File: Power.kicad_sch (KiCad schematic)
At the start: 18 parts, among them J4 Conn_01x02, SW2 SW_Push, U6 NPM1300-QEAA-R7

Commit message: Switch inductors
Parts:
- removed L1, L2: LQM2HPN2R2MG0L, LQM:IND_LQM2HPN2R2MG0L_MUR, symbol 2026-04-16_01-05-19:LQM2HPN2R2MG0L
- added L3, L4: 2.2uH, Inductor_SMD:L_0805_2012Metric, symbol Device:L_Small
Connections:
- net +1V8: now also L3.1
- net +3V0: now also L4.1
- net SW1: now also L3.2
- net SW2: now also L4.2

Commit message: WIP changes
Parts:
- SW2: footprint SKRPACE:SW_SKRPACE010_AAL -> Resistor_SMD:R_0805_2012Metric
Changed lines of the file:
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@@
 			)
 		)
-		(property "Footprint" "SKRPACE:SW_SKRPACE010_AAL"
+		(property "Footprint" "Resistor_SMD:R_0805_2012Metric"
 			(at 77.47 119.38 0)
 			(hide yes)

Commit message: Added Backpack Integration + Layout V1
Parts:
- SW2: now left out of the parts list

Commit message: Began Backpack Removal to Lower Profile
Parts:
- C10, C22: Price 0.008USD -> (none)
- C11, C16, C17, C18, C19, C20: Price 0.009USD -> (none)
- C15: Price 0.006USD -> (none)
- R12, R13: Price 0.004USD -> (none)

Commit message: Flipped switches + Heart Rate, Moving Battery
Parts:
- J4: footprint Connector_JST:JST_PH_S2B-PH-K_1x02_P2.00mm_Horizontal -> Smart_Watch:MOLEX_0781710002
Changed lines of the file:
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@@
 			)
 		)
-		(property "Footprint" "Connector_JST:JST_PH_S2B-PH-K_1x02_P2.00mm_Horizontal"
+		(property "Footprint" "Smart_Watch:MOLEX_0781710002"
 			(at 49.53 76.2 0)
 			(hide yes)

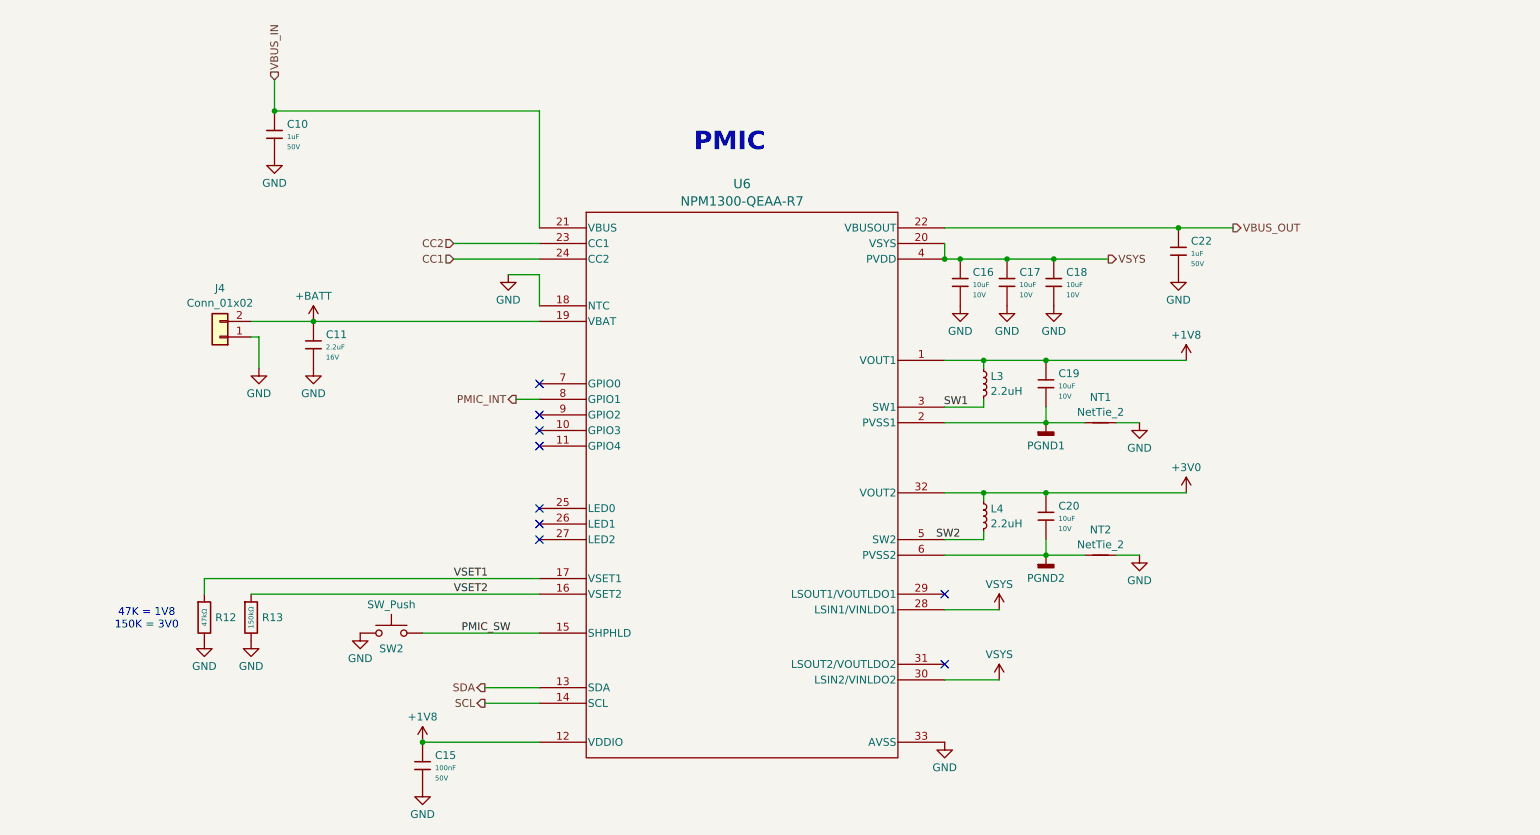
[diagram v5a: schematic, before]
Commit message: Added Test Points and Changed to Top Mounted USBC
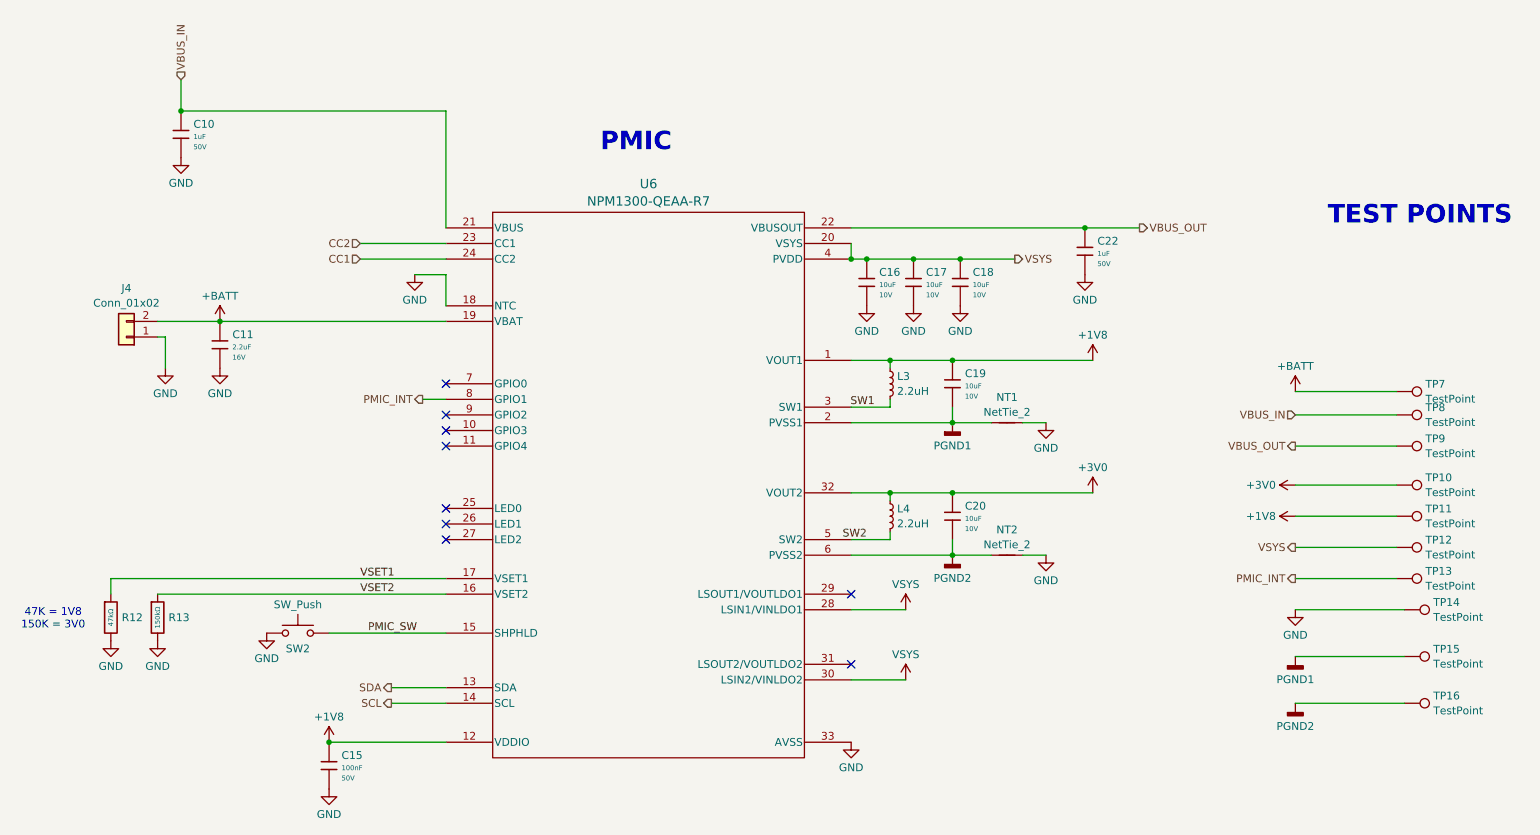
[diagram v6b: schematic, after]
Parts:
- added TP10, TP11, TP12, TP13, TP14, TP15, TP16, TP7, TP8, TP9: TestPoint, TestPoint:TestPoint_Pad_1.0x1.0mm, symbol Connector:TestPoint
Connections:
- net +1V8: now also TP11.1
- net +3V0: now also TP10.1
- net +BATT: now also TP7.1
- net GND: now also TP14.1
- net PGND1: now also TP15.1
- net PGND2: now also TP16.1
- net PMIC_INT: now also TP13.1
- net VBUS_IN: now also TP8.1
- net VBUS_OUT: now also TP9.1
- net VSYS: now also TP12.1
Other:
- note added: "TEST POINTS"
- moved on the sheet: C10, C11, C15, C16, C17, C18, C19, C20, C22, J4, L3, L4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

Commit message: Fix some ERC problems
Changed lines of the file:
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@@
 	)
 	(junction
+		(at 59.69 73.66)
+		(diameter 0)
+		(color 0 0 0 0)
+	)
+	(junction
 		(at 152.4 63.5)
 		(diameter 0)
@@
 	(wire
 		(pts
+			(xy 59.69 73.66) (xy 86.36 73.66)
+		)
+		(stroke
+			(width 0)
+			(type default)
+		)
+	)
+	(wire
+		(pts
 			(xy 168.91 109.22) (xy 168.91 111.76)
 		)
@@
 	(wire
 		(pts
+			(xy 49.53 71.12) (xy 49.53 73.66)
+		)
+		(stroke
+			(width 0)
+			(type default)
+		)
+	)
+	(wire
+		(pts
 			(xy 81.28 66.04) (xy 86.36 66.04)
 		)
@@
 	(wire
 		(pts
-			(xy 49.53 73.66) (xy 86.36 73.66)
+			(xy 49.53 73.66) (xy 59.69 73.66)
 		)
 		(stroke
@@
 	)
 	(symbol
+		(lib_id "power:PWR_FLAG")
+		(at 59.69 73.66 0)
+		(unit 1)
+		(body_style 1)
+		(exclude_from_sim no)
+		(in_bom yes)
+		(on_board yes)
+		(in_pos_files yes)
+		(dnp no)
+		(fields_autoplaced yes)
+		(property "Reference" "#FLG01"
+			(at 59.69 71.755 0)
+			(hide yes)
+			(show_name no)
+			(do_not_autoplace no)
+			(effects
+				(font
+					(size 1.27 1.27)
+				)
+			)
+		)
+		(property "Value" "PWR_FLAG"
+			(at 59.69 69.5269 0)
+			(show_name no)
+			(do_not_autoplace no)
+			(effects
+				(font
+					(size 1.27 1.27)
+				)
+			)
+		)
+		(property "Footprint" ""
+			(at 59.69 73.66 0)
+			(hide yes)
+			(show_name no)
+			(do_not_autoplace no)
+			(effects
+				(font
+					(size 1.27 1.27)
+				)
+			)
+		)
+		(property "Datasheet" ""
+			(at 59.69 73.66 0)
+			(hide yes)
+			(show_name no)
+			(do_not_autoplace no)
+			(effects
+				(font
+					(size 1.27 1.27)
+				)
+			)
+		)
+		(property "Description" "Special symbol for telling ERC where power comes from"
+			(at 59.69 73.66 0)
+			(hide yes)
+			(show_name no)
+			(do_not_autoplace no)
+			(effects
+				(font
+					(size 1.27 1.27)
+				)
+			)
+		)
+		(pin "1"
+		)
+		(instances
+			(project "Smart_Watch"
+				(path "/69095a4d-0a57-4fa3-aecb-1cfd89eedc11/bed567dd-6d09-419a-b99a-3e57c9439bd4/88559da1-41ec-4d01-a245-44d6dbccae3b"
+					(reference "#FLG01")
+					(unit 1)
+				)
+			)
+		)
+	)
+	(symbol
 		(lib_id "power:GND")
 		(at 184.15 90.17 0)
@@
 			)
 		)
-		(property "Check_prices" ""
-			(at 119.38 100.33 0)
-			(hide yes)
-			(show_name no)
-			(do_not_autoplace no)
-			(effects
-				(font
-					(size 1.27 1.27)
-				)
-			)
-		)
-		(property "Description_1" ""
-			(at 119.38 100.33 0)
-			(hide yes)
-			(show_name no)
-			(do_not_autoplace no)
-			(effects
-				(font
-					(size 1.27 1.27)
-				)
-			)
-		)
-		(property "Inductance" ""
-			(at 119.38 100.33 0)
-			(hide yes)
-			(show_name no)
-			(do_not_autoplace no)
-			(effects
-				(font
-					(size 1.27 1.27)
-				)
-			)
-		)
-		(property "MF" ""
-			(at 119.38 100.33 0)
-			(hide yes)
-			(show_name no)
-			(do_not_autoplace no)
-			(effects
-				(font
-					(size 1.27 1.27)
-				)
-			)
-		)
-		(property "MP" ""
-			(at 119.38 100.33 0)
-			(hide yes)
-			(show_name no)
-			(do_not_autoplace no)
-			(effects
-				(font
-					(size 1.27 1.27)
-				)
-			)
-		)
-		(property "Purchase-URL" ""
-			(at 119.38 100.33 0)
-			(hide yes)
-			(show_name no)
-			(do_not_autoplace no)
-			(effects
-				(font
-					(size 1.27 1.27)
-				)
-			)
-		)
-		(property "SnapEDA_Link" ""
-			(at 119.38 100.33 0)
-			(hide yes)
-			(show_name no)
-			(do_not_autoplace no)
-			(effects
-				(font
-					(size 1.27 1.27)
-				)
-			)
-		)
 		(pin "7"
 		)
@@
 	(symbol
 		(lib_id "power:+BATT")
-		(at 49.53 73.66 0)
+		(at 49.53 71.12 0)
 		(unit 1)
 		(body_style 1)
@@
 		(fields_autoplaced yes)
 		(property "Reference" "#PWR030"
-			(at 49.53 77.47 0)
+			(at 49.53 74.93 0)
 			(hide yes)
 			(show_name no)
@@
 		)
 		(property "Value" "+BATT"
-			(at 49.53 69.5269 0)
+			(at 49.53 66.9869 0)
 			(show_name no)
 			(do_not_autoplace no)
@@
 		)
 		(property "Footprint" ""
-			(at 49.53 73.66 0)
+			(at 49.53 71.12 0)
 			(hide yes)
 			(show_name no)
@@
 		)
 		(property "Datasheet" ""
-			(at 49.53 73.66 0)
+			(at 49.53 71.12 0)
 			(hide yes)
 			(show_name no)
@@
 		)
 		(property "Description" "Power symbol creates a global label with name \"+BATT\""
-			(at 49.53 73.66 0)
+			(at 49.53 71.12 0)
 			(hide yes)
 			(show_name no)

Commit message: New Case Files + Updated DRC Errors
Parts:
- renumbered TP11 to +1V8, TP10 to +3V0, TP7 to +BATT1, TP14 to GND1, TP15 to PGND1, TP16 to PGND2, TP13 to PMIC_INT1, TP8 to VBUS_IN1, TP9 to VBUS_OUT1, TP12 to VSYS1
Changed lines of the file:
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@@
 		(dnp no)
 		(fields_autoplaced yes)
-		(property "Reference" "TP11"
+		(property "Reference" "+1V8"
 			(at 245.999 104.1978 90)
 			(show_name no)
@@
 			(project "Smart_Watch"
 				(path "/69095a4d-0a57-4fa3-aecb-1cfd89eedc11/bed567dd-6d09-419a-b99a-3e57c9439bd4/88559da1-41ec-4d01-a245-44d6dbccae3b"
-					(reference "TP11")
+					(reference "+1V8")
 					(unit 1)
 				)
@@
 		(dnp no)
 		(fields_autoplaced yes)
-		(property "Reference" "TP12"
+		(property "Reference" "VSYS1"
 			(at 245.999 109.2778 90)
 			(show_name no)
@@
 			(project "Smart_Watch"
 				(path "/69095a4d-0a57-4fa3-aecb-1cfd89eedc11/bed567dd-6d09-419a-b99a-3e57c9439bd4/88559da1-41ec-4d01-a245-44d6dbccae3b"
-					(reference "TP12")
+					(reference "VSYS1")
 					(unit 1)
 				)
@@
 		(dnp no)
 		(fields_autoplaced yes)
-		(property "Reference" "TP15"
+		(property "Reference" "PGND1"
 			(at 247.269 127.0578 90)
 			(show_name no)
@@
 			(project "Smart_Watch"
 				(path "/69095a4d-0a57-4fa3-aecb-1cfd89eedc11/bed567dd-6d09-419a-b99a-3e57c9439bd4/88559da1-41ec-4d01-a245-44d6dbccae3b"
-					(reference "TP15")
+					(reference "PGND1")
 					(unit 1)
 				)
@@
 		(dnp no)
 		(fields_autoplaced yes)
-		(property "Reference" "TP13"
+		(property "Reference" "PMIC_INT1"
 			(at 245.999 114.3578 90)
 			(show_name no)
@@
 			(project "Smart_Watch"
 				(path "/69095a4d-0a57-4fa3-aecb-1cfd89eedc11/bed567dd-6d09-419a-b99a-3e57c9439bd4/88559da1-41ec-4d01-a245-44d6dbccae3b"
-					(reference "TP13")
+					(reference "PMIC_INT1")
 					(unit 1)
 				)
@@
 		(dnp no)
 		(fields_autoplaced yes)
-		(property "Reference" "TP10"
+		(property "Reference" "+3V0"
 			(at 245.999 99.1178 90)
 			(show_name no)
@@
 			(project "Smart_Watch"
 				(path "/69095a4d-0a57-4fa3-aecb-1cfd89eedc11/bed567dd-6d09-419a-b99a-3e57c9439bd4/88559da1-41ec-4d01-a245-44d6dbccae3b"
-					(reference "TP10")
+					(reference "+3V0")
 					(unit 1)
 				)
@@
 		(dnp no)
 		(fields_autoplaced yes)
-		(property "Reference" "TP16"
+		(property "Reference" "PGND2"
 			(at 247.269 134.6778 90)
 			(show_name no)
@@
 			(project "Smart_Watch"
 				(path "/69095a4d-0a57-4fa3-aecb-1cfd89eedc11/bed567dd-6d09-419a-b99a-3e57c9439bd4/88559da1-41ec-4d01-a245-44d6dbccae3b"
-					(reference "TP16")
+					(reference "PGND2")
 					(unit 1)
 				)
@@
 		(dnp no)
 		(fields_autoplaced yes)
-		(property "Reference" "TP8"
+		(property "Reference" "VBUS_IN1"
 			(at 245.999 87.6878 90)
 			(show_name no)
@@
 			(project "Smart_Watch"
 				(path "/69095a4d-0a57-4fa3-aecb-1cfd89eedc11/bed567dd-6d09-419a-b99a-3e57c9439bd4/88559da1-41ec-4d01-a245-44d6dbccae3b"
-					(reference "TP8")
+					(reference "VBUS_IN1")
 					(unit 1)
 				)
@@
 		(dnp no)
 		(fields_autoplaced yes)
-		(property "Reference" "TP14"
+		(property "Reference" "GND1"
 			(at 247.269 119.4378 90)
 			(show_name no)
@@
 			(project "Smart_Watch"
 				(path "/69095a4d-0a57-4fa3-aecb-1cfd89eedc11/bed567dd-6d09-419a-b99a-3e57c9439bd4/88559da1-41ec-4d01-a245-44d6dbccae3b"
-					(reference "TP14")
+					(reference "GND1")
 					(unit 1)
 				)
@@
 		(dnp no)
 		(fields_autoplaced yes)
-		(property "Reference" "TP7"
+		(property "Reference" "+BATT1"
 			(at 245.999 83.8778 90)
 			(show_name no)
@@
 			(project "Smart_Watch"
 				(path "/69095a4d-0a57-4fa3-aecb-1cfd89eedc11/bed567dd-6d09-419a-b99a-3e57c9439bd4/88559da1-41ec-4d01-a245-44d6dbccae3b"
-					(reference "TP7")
+					(reference "+BATT1")
 					(unit 1)
 				)
@@
 		(dnp no)
 		(fields_autoplaced yes)
-		(property "Reference" "TP9"
+		(property "Reference" "VBUS_OUT1"
 			(at 245.999 92.7678 90)
 			(show_name no)
@@
 			(project "Smart_Watch"
 				(path "/69095a4d-0a57-4fa3-aecb-1cfd89eedc11/bed567dd-6d09-419a-b99a-3e57c9439bd4/88559da1-41ec-4d01-a245-44d6dbccae3b"
-					(reference "TP9")
+					(reference "VBUS_OUT1")
 					(unit 1)
 				)
